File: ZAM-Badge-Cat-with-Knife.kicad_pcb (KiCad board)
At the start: 2 copper layers, 65.5 x 57.5 mm, 4 parts, among them SW101 SW_SPDT

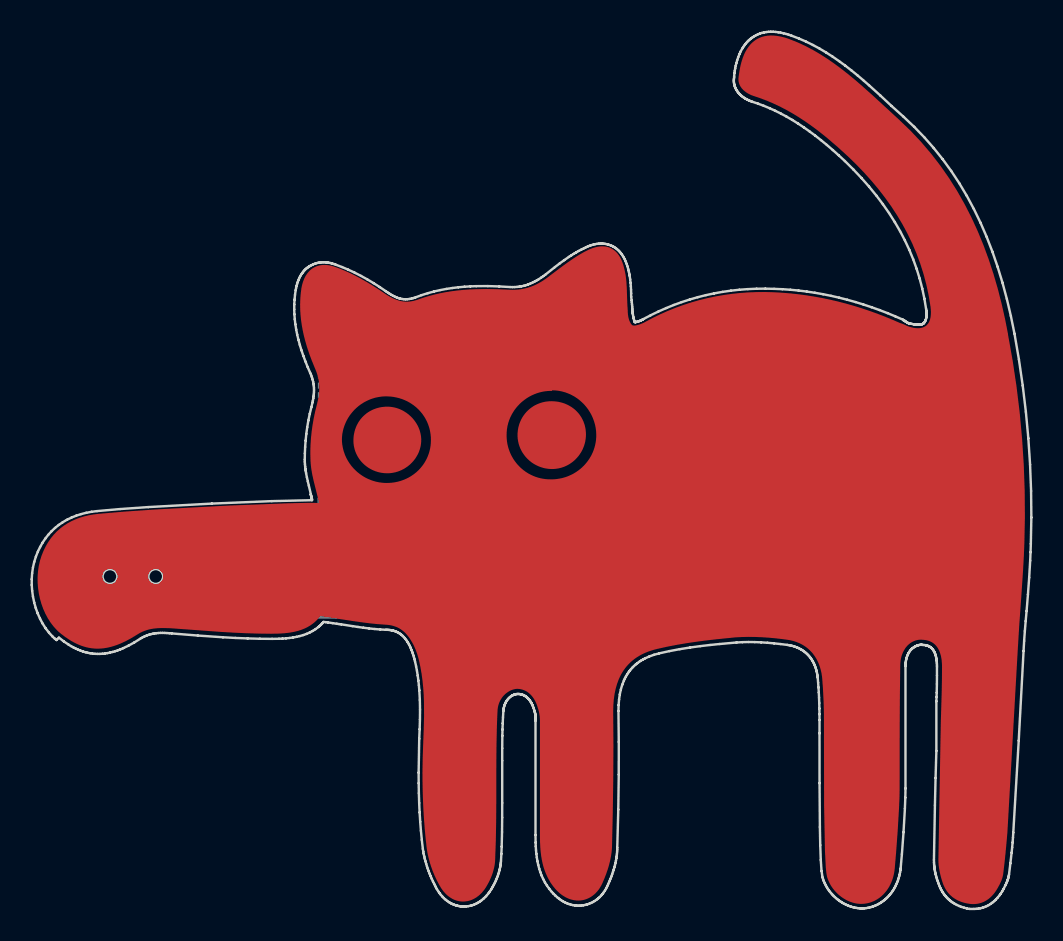
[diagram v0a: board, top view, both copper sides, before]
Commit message: Finalise the layout and add ZAM logo and a placeholder for the butterfly pin
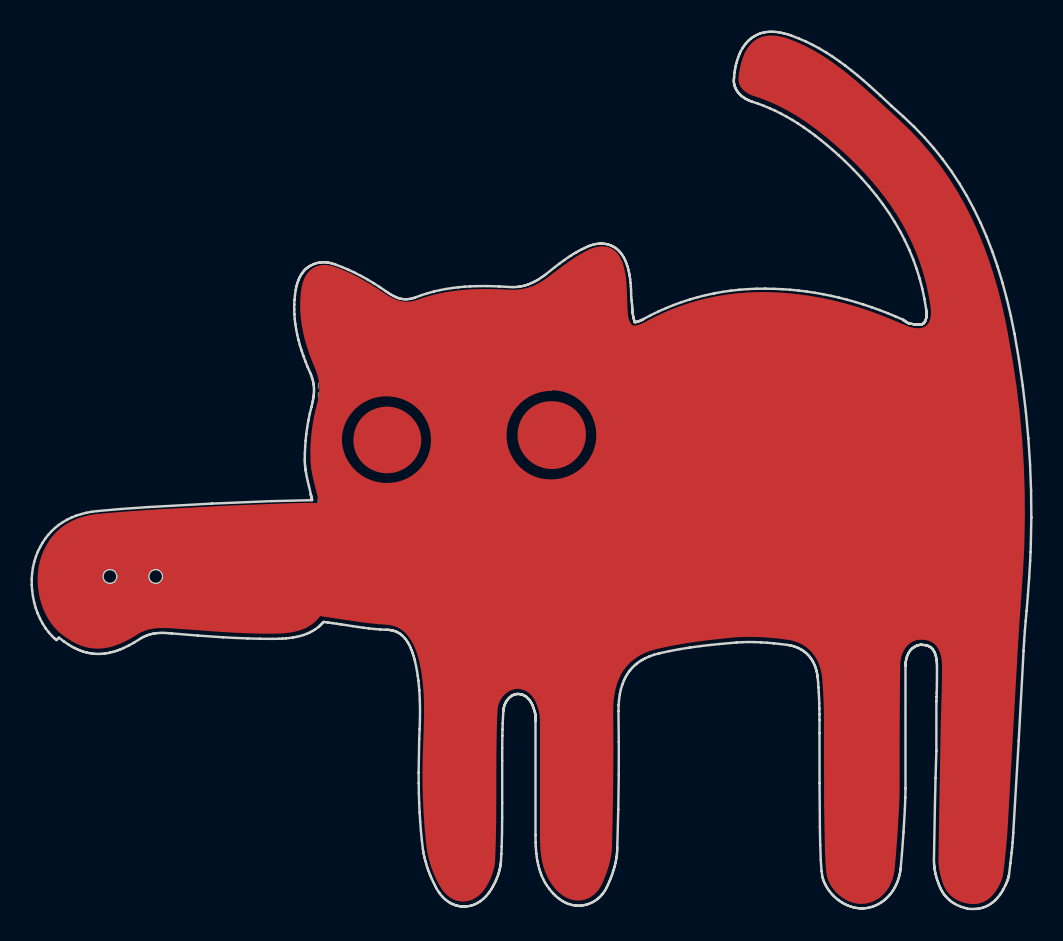
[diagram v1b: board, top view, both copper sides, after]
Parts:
- added Lg101: logo, Cat-with-Knife:ZAM_LOGO_440, B.Cu at (144.3, 99.7)
- added Lg102: logo, Cat-with-Knife:Butterfy-Pin, B.Cu at (152.4, 75.9)
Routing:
- net Net-(BT101-+): track 74.1 -> 71.8 mm
- net Net-(D101-A): track 33.2 -> 34.6 mm
